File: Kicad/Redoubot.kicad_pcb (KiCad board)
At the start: 4 copper layers, 99 parts, among them J1 HM_10_BLE_Module, J10 VL53L0CXV0DH - TOF, J11 DFPlayer_Left, J12 Speaker, J13 DFPlayer_Right, J14 USB_C_Receptacle_USB2.0_16P, J15 Conn_ST_STDC14, J2 Connecteur batterie, J3 APDS9960, J4 Neopixel, J5 Motor_Left, J6 Motor_Right, J7 MPU-6050, J8 Servo_Left, J9 Servo_Right, Q1 DMP1045UQ-7, U1 STM32G431RBTx, U2 LD39050PU33R, U3 BQ25896RTWR, U4 BQ27220YZFR, U5 DRV8833PWP, U6 USBLC6-2SC6, U7 DMN313DLT-7, U8 MMDT2907A-7-F, Y1 8MHz

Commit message: feat: started routing, notably connecting the GNDs
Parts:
- moved C15 19.0 mm to (140.5, 36.0), turned to 180 degrees
- moved C1 14.9 mm to (189.2, 101.5)
- moved C2 14.9 mm to (189.2, 103.5)
- moved Y1 14.9 mm to (195.5, 102.2)
- moved R18 13.5 mm to (137.5, 34.0), turned to -90 degrees
- moved C14 12.0 mm to (143.5, 33.0)
- moved C3 8.44 mm to (192.5, 59.5), turned to 180 degrees
- moved C13 8.36 mm to (144.0, 34.5)
- moved C4 6.40 mm to (198.5, 63.0)
- moved R14 3.59 mm to (131.5, 33.0)
- moved JP1 2.96 mm to (187.0, 57.0), turned to 180 degrees
- moved C27 0.40 mm to (201.5, 100.6)
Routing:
- net GND: track 0.00 -> 120.0 mm, vias 0 -> 83
- net +3.3V: track 0.00 -> 24.2 mm
- net Net-(U1-PF1): track 0.00 -> 22.7 mm
- net Net-(U1-PF0): track 0.00 -> 16.9 mm
- net Net-(U4-VDD): track 0.00 -> 3.85 mm
- net /STM32/NRST: track 0.00 -> 2.57 mm
- net Net-(JP2-A): track 0.00 -> 1.90 mm
- net /Power_management/BAT: track 0.00 -> 1.59 mm
- net Net-(JP1-A): track 0.00 -> 1.58 mm

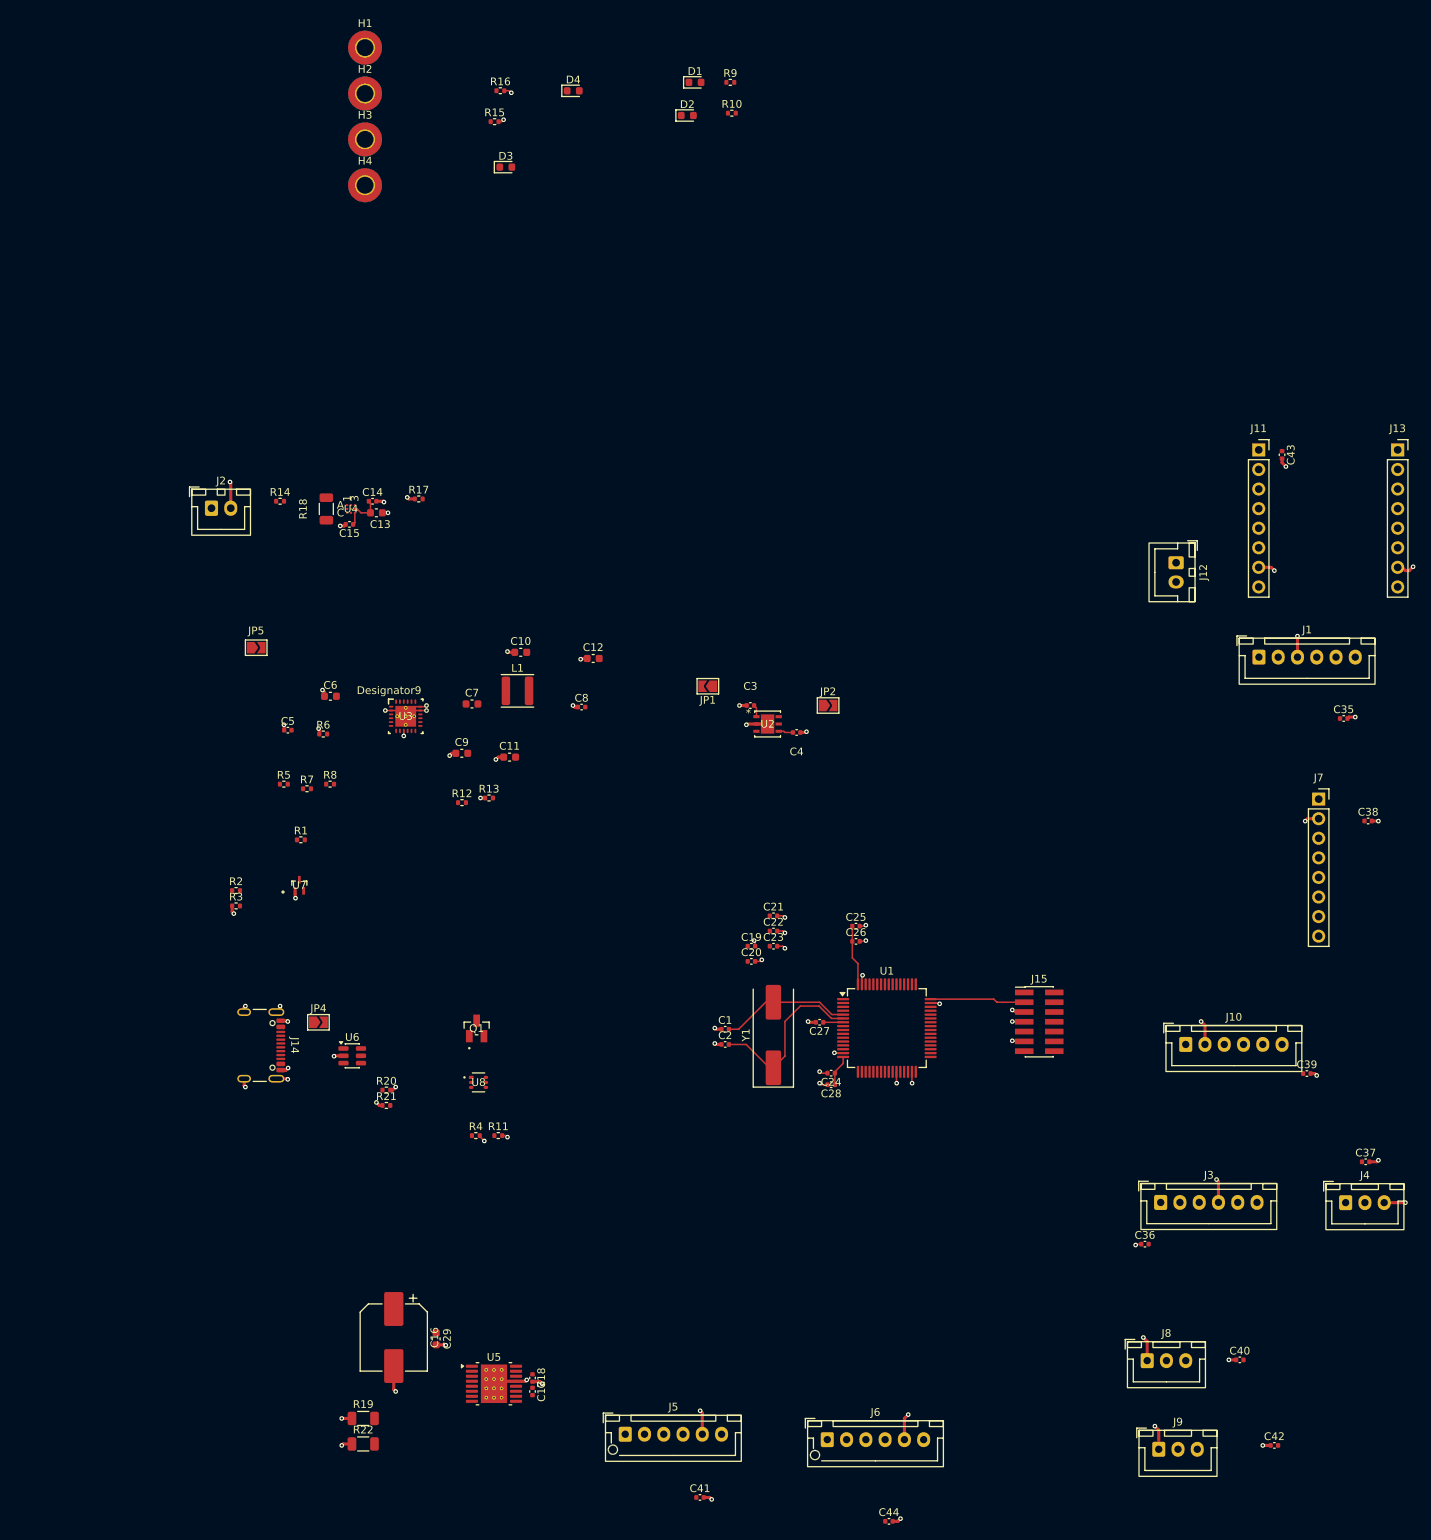
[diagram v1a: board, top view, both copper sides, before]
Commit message: chore: redid placement from the ground up
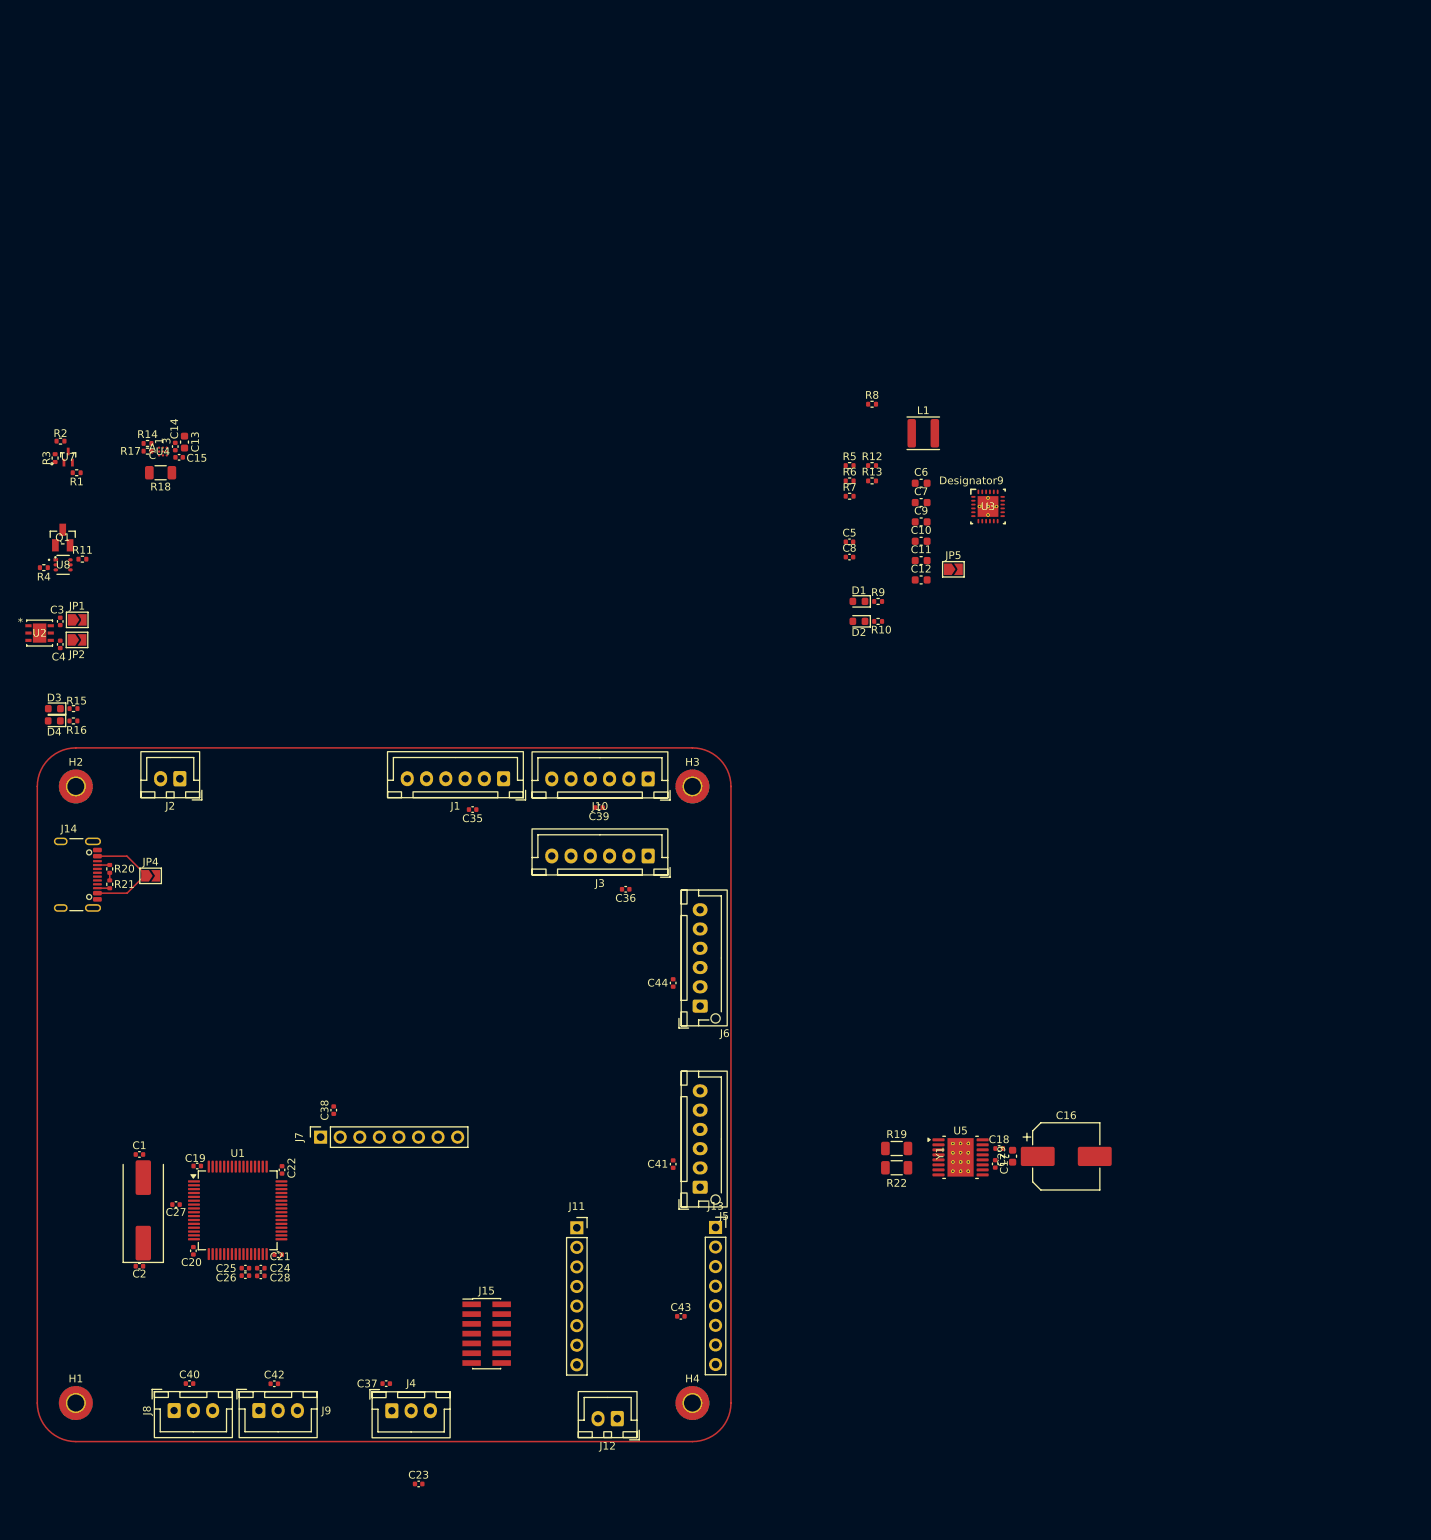
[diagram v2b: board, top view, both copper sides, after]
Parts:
- removed U6: USBLC6-2SC6, Package_TO_SOT_SMD:SOT-23-6
- moved H1 179.8 mm to (105.0, 150.0)
- moved H4 163.6 mm to (185.0, 150.0)
- moved C38 139.4 mm to (138.5, 112.0), turned to 90 degrees
- moved J7 136.7 mm to (136.8, 115.5), turned to 90 degrees
- moved C40 136.3 mm to (119.8, 147.5)
- moved C43 136.3 mm to (183.5, 138.8), turned to 0 degrees
- moved J11 134.2 mm to (170.0, 127.3)
- moved J13 134.2 mm to (188.0, 127.2)
- moved J12 132.6 mm to (175.2, 152.0), turned to 180 degrees
- moved C37 130.3 mm to (145.3, 147.5), turned to 180 degrees
- moved C42 130.0 mm to (130.8, 147.5)
- moved J4 126.7 mm to (146.0, 151.0)
- moved J8 126.4 mm to (117.8, 151.0)
- moved J9 116.9 mm to (128.8, 151.0)
- moved C35 113.6 mm to (156.5, 73.0), turned to 180 degrees
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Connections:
- J14 pad A6: /Power_management/D+ -> unconnected-(J14-D+-PadA6)
- J14 pad A7: /Power_management/D- -> unconnected-(J14-D--PadA7)
- J14 pad B6: /Power_management/D+ -> unconnected-(J14-D+-PadB6)
- J14 pad B7: /Power_management/D- -> unconnected-(J14-D--PadB7)
- U1 pad 45: /USB_DM -> unconnected-(U1-PA11-Pad45)
- U1 pad 46: /USB_DP -> unconnected-(U1-PA12-Pad46)
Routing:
- net GND: track 120.0 -> 0.98 mm, vias 83 -> 0
- net +3.3V: track 24.2 -> 0.00 mm
- net Net-(U1-PF1): track 22.7 -> 0.00 mm
- net Net-(U1-PF0): track 16.9 -> 0.00 mm
- net Net-(JP4-A): track 0.00 -> 14.5 mm
- net Net-(U4-VDD): track 3.85 -> 0.00 mm
- net /STM32/NRST: track 2.57 -> 0.00 mm
- net Net-(JP2-A): track 1.90 -> 0.00 mm
- net Net-(J14-CC1): track 0.00 -> 1.60 mm
- net Net-(J14-CC2): track 0.00 -> 1.60 mm
- net /Power_management/BAT: track 1.59 -> 0.00 mm
- net Net-(JP1-A): track 1.58 -> 0.00 mm
- removed copper zone on In2.Cu, net +3.3V
- removed copper zone on In2.Cu, net +5V
- removed copper zone on In1.Cu, net GND
